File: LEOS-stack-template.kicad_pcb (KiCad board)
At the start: 2 copper layers, 100 x 100 mm, 19 parts, among them J1 MicroFit_1x4, J2 MicroFit_1x4, U1 MCP2562FD, U2 MCP2518FD, Y1 40 MHz

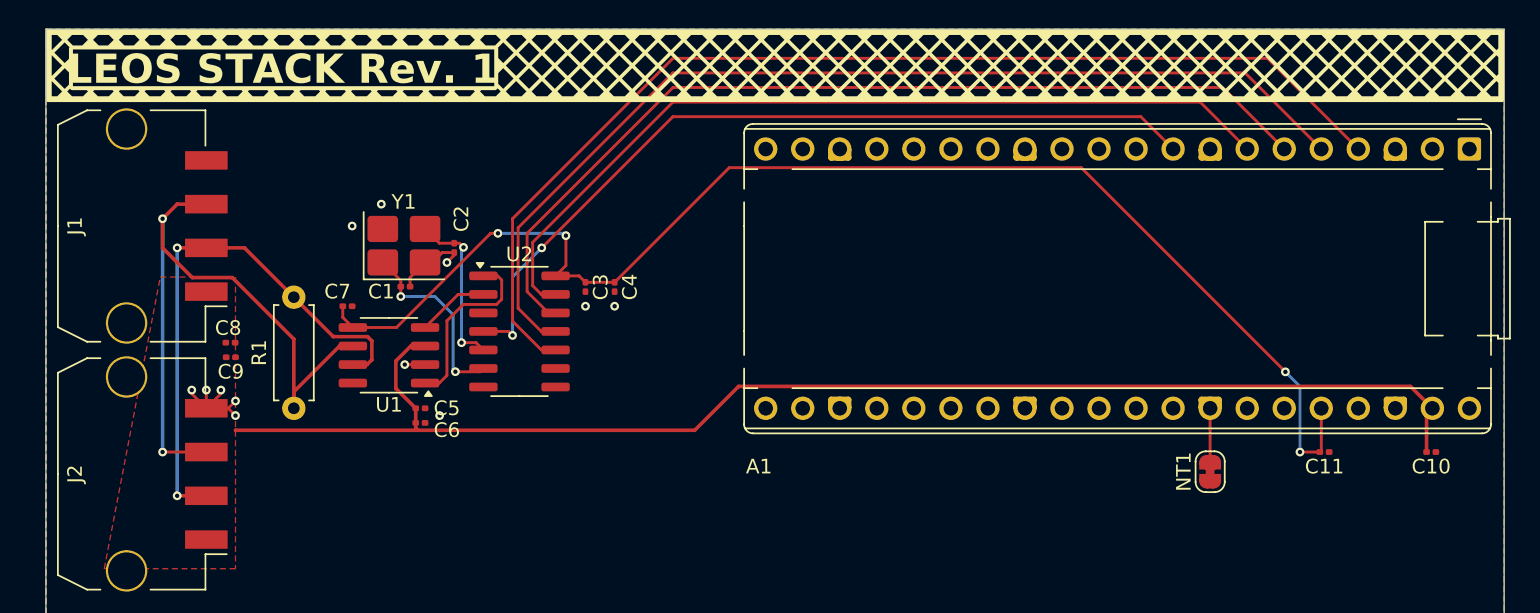
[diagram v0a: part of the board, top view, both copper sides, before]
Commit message: Redesigned Rev 2 fixing 0603 cap size and layout
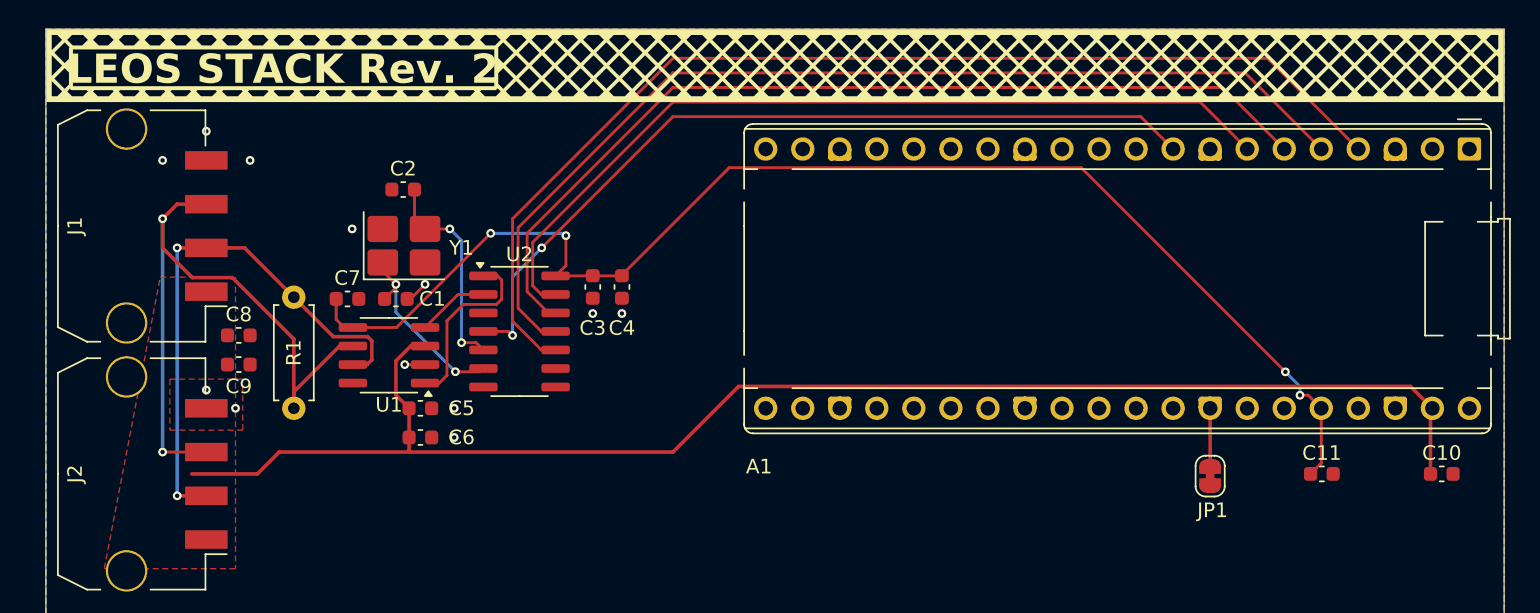
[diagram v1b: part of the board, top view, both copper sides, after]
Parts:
- removed NT1: NetTie_2, Jumper:SolderJumper-2_P1.3mm_Bridged_RoundedPad1.0x1.5mm
- added JP1: AGND Tie, Jumper:SolderJumper-2_P1.3mm_Bridged_RoundedPad1.0x1.5mm, F.Cu at (179.8, 80.7)
- C1, C10, C11, C2, C3, C4, C5, C6, C7, C8, C9: footprint Capacitor_SMD:C_0201_0603Metric -> Capacitor_SMD:C_0603_1608Metric
- moved C2 5.32 mm to (124.5, 61.0), turned to 0 degrees
- moved C10 1.67 mm to (195.7, 80.5)
- moved C11 1.51 mm to (187.5, 80.5)
- moved C1 1.07 mm to (124.0, 68.5)
- moved C6 1.00 mm to (125.7, 78.0)
- moved C8 0.76 mm to (113.2, 71.0)
- moved C9 0.74 mm to (113.2, 73.0)
- moved C3 0.50 mm to (137.5, 67.7)
- moved C4 0.50 mm to (139.5, 67.7)
- moved C7 0.50 mm to (120.7, 68.5)
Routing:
- net GND: track 14.1 -> 4.24 mm
- net +5V: track 94.9 -> 102.2 mm
- net /OSC2: track 11.5 -> 15.3 mm
- net VDD: track 91.8 -> 90.8 mm
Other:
- board text added: "LEOS STACK Rev. 2"
- board text removed: "LEOS STACK Rev. 1"

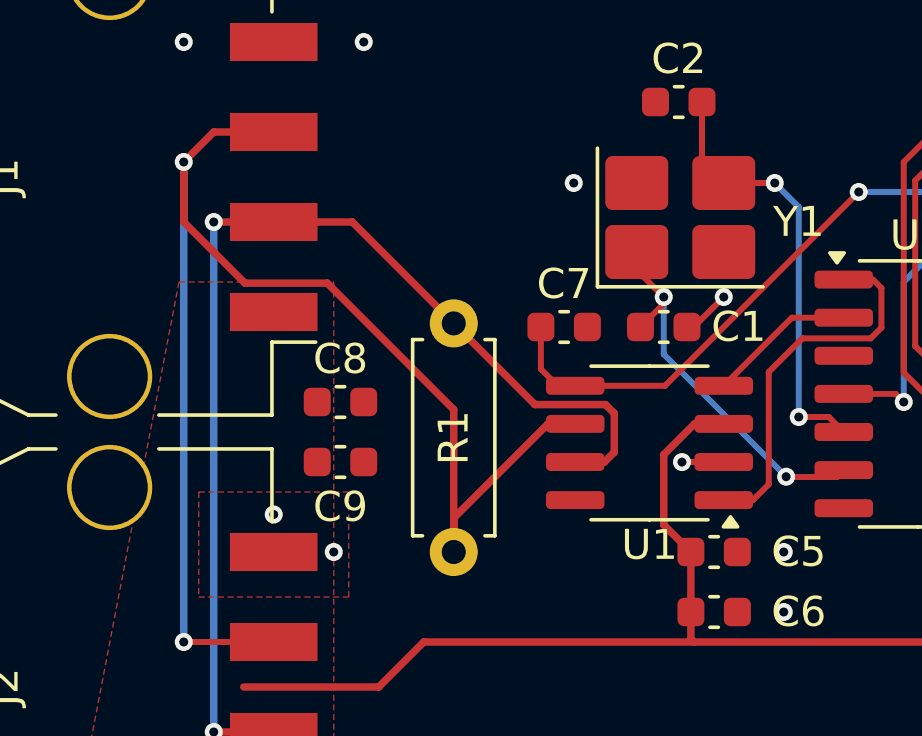
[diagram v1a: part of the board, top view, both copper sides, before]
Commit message: Clean up tracks to remove warnings
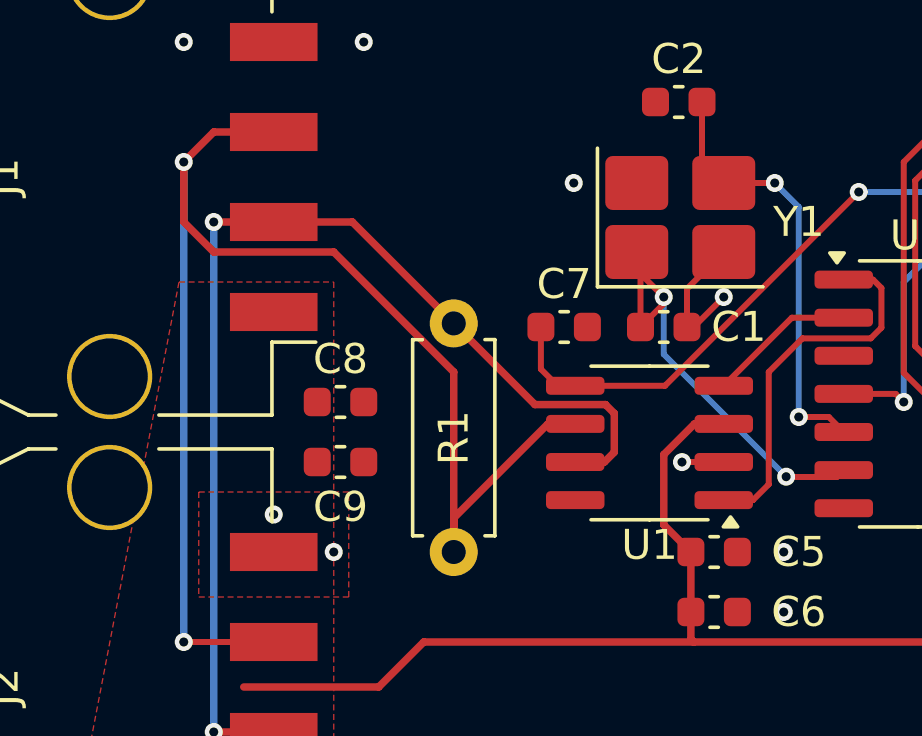
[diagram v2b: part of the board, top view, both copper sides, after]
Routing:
- net /OSC1: track 12.9 -> 15.4 mm
- net GND: track 4.24 -> 6.54 mm
- net /OSC2: track 15.3 -> 14.5 mm
- net /CAN-: track 47.2 -> 48.0 mm
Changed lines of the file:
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@@
+	)
+	(segment
+		(start 124.775 68.5)
+		(end 124.775 67.225)
+		(width 0.2)
+		(layer "F.Cu")
+		(net 13)
 	)
 	(segment
@@
 	)
 	(segment
-		(start 126.5 66.5)
-		(end 126 66)
-		(width 0.2)
-		(layer "F.Cu")
-		(net 13)
-	)
-	(segment
 		(start 124.775 68.5)
 		(end 125 68.5)
@@
 		(net 13)
 	)
+	(segment
+		(start 124.775 67.225)
+		(end 126 66)
+		(width 0.2)
+		(layer "F.Cu")
+		(net 13)
+	)
 	(via
 		(at 128 76)
@@
 	)
 	(segment
-		(start 125 76)
-		(end 125.18 75.82)
-		(width 0.25)
-		(layer "F.Cu")
-		(net 34)
-	)
-	(segment
 		(start 125 79)
 		(end 143 79)
@@
 	)
 	(segment
-		(start 124.905 76)
-		(end 125 76)
-		(width 0.25)
-		(layer "F.Cu")
-		(net 34)
-	)
-	(segment
 		(start 116 79)
 		(end 114.5 80.5)
@@
 	)
 	(segment
+		(start 123.225 66.125)
+		(end 123.1 66)
+		(width 0.2)
+		(layer "F.Cu")
+		(net 35)
+	)
+	(segment
 		(start 123.1 66)
 		(end 123.1 66.6)
@@
 	)
 	(segment
+		(start 123.225 68.5)
+		(end 123.225 66.125)
+		(width 0.2)
+		(layer "F.Cu")
+		(net 35)
+	)
+	(segment
 		(start 128.090209 73.5)
 		(end 129.77 73.5)
@@
 	)
 	(segment
-		(start 126.525 64.225)
-		(end 126 63.7)
-		(width 0.2)
-		(layer "F.Cu")
-		(net 36)
-	)
-	(segment
 		(start 125.275 61)
 		(end 125.275 62.975)
@@
 	)
 	(segment
+		(start 113 66)
+		(end 117 70)
+		(width 0.25)
+		(layer "F.Cu")
+		(net 38)
+	)
+	(segment
 		(start 111 62)
 		(end 109 62)
@@
 	)
 	(segment
-		(start 117 71.253)
-		(end 117 76)
-		(width 0.25)
-		(layer "F.Cu")
-		(net 38)
-	)
-	(segment
 		(start 117 74.86863)
 		(end 120.13863 71.73)
@@
 	)
 	(segment
-		(start 110.039 67.039)
-		(end 112.786 67.039)
-		(width 0.25)
-		(layer "F.Cu")
-		(net 38)
-	)
-	(segment
-		(start 108 65)
-		(end 110.039 67.039)
+		(start 117 70)
+		(end 117 76)
+		(width 0.25)
+		(layer "F.Cu")
+		(net 38)
+	)
+	(segment
+		(start 108 63)
+		(end 108 65)
 		(width 0.25)
 		(layer "F.Cu")
@@
 	)
 	(segment
-		(start 112.786 67.039)
-		(end 117 71.253)
-		(width 0.25)
-		(layer "F.Cu")
-		(net 38)
-	)
-	(segment
 		(start 120.13863 71.73)
 		(end 121.05 71.73)
@@
 	)
 	(segment
-		(start 108 63)
-		(end 108 65)
+		(start 109 66)
+		(end 113 66)
+		(width 0.25)
+		(layer "F.Cu")
+		(net 38)
+	)
+	(segment
+		(start 108 65)
+		(end 109 66)
 		(width 0.25)
 		(layer "F.Cu")
@@
 		(net_name "")
 		(layers "*.SilkS")
-		(hatch full 0.5)
+		(hatch edge 0.5)
 		(connect_pads
 			(clearance 0)

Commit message: New redesign featuring updated components, new sheets, better routing, and 100% 3D View
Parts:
- removed JP1: AGND Tie, Jumper:SolderJumper-2_P1.3mm_Bridged_RoundedPad1.0x1.5mm
- added TP1: CAN-H Test Point, TestPoint:TestPoint_Loop_D2.60mm_Drill0.9mm_Beaded, F.Cu at (117.0, 79.0)
- added TP2: CAN-L Test Point, TestPoint:TestPoint_Loop_D2.60mm_Drill0.9mm_Beaded, F.Cu at (117.0, 65.0)
- added TP3: 5V Test Point, TestPoint:TestPoint_Loop_D2.60mm_Drill0.9mm_Beaded, F.Cu at (117.0, 85.0)
- added TP4: GND Test Point, TestPoint:TestPoint_Loop_D2.60mm_Drill0.9mm_Beaded, F.Cu at (117.0, 59.0)
- A1: value RaspberryPi_Pico -> RaspberryPi Pico
- C1, C2: value 12pF -> 15p
- C10, C3, C5, C7: value 0.1uF -> 0.1u
- C11: value 10uF -> 10u; footprint Capacitor_SMD:C_0603_1608Metric -> Capacitor_SMD:C_0805_2012Metric
- C4, C6: value 1uF -> 1u
- C8: value 47uF -> 22u; footprint Capacitor_SMD:C_0603_1608Metric -> Capacitor_SMD:C_0805_2012Metric
- C9: value 0.1uF -> 22u; footprint Capacitor_SMD:C_0603_1608Metric -> Capacitor_SMD:C_0805_2012Metric
- J1, J2: footprint Connector_Molex:Molex_Micro-Fit_3.0_43650-0410_1x04-1MP_P3.00mm_Horizontal_PnP -> LEOS:Molex_MicroFit3.0_43650-0410_1x04_Horizontal
- R1: value 120R -> 120
- Y1: footprint Crystal:Crystal_SMD_3225-4Pin_3.2x2.5mm_HandSoldering -> Crystal:Crystal_SMD_2016-4Pin_2.0x1.6mm
- moved R1 7.81 mm to (117.0, 68.2), turned to -90 degrees
- moved C2 2.51 mm to (124.7, 63.5)
- moved C11 1.12 mm to (188.5, 80.0)
- moved Y1 1.11 mm to (124.7, 66.0)
- moved C10 0.50 mm to (195.8, 80.0)
- moved C8 0.50 mm to (113.2, 70.5)
- moved C9 0.50 mm to (113.2, 73.5)
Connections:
- net /CAN+ renamed /CANbus/CAN+
- net /CAN- renamed /CANbus/CAN-
- net /CAN_CS renamed /CANbus/CS
- net /CAN_INT renamed /CANbus/INT
- net /CAN_MISO renamed /CANbus/MISO
- net /CAN_MOSI renamed /CANbus/MOSI
- net /CAN_SCK renamed /CANbus/SCK
- net /OSC2 renamed /CANbus/OSC2
- net /RXCAN renamed Net-(U1-RXD)
- net /TXCAN renamed Net-(U1-TXD)
- A1 pad 1: UART0_TX -> unconnected-(A1-GPIO0-Pad1)
- A1 pad 10: GP7 -> unconnected-(A1-GPIO7-Pad10)
- A1 pad 11: I2C0_SDA -> unconnected-(A1-GPIO8-Pad11)
- A1 pad 12: I2C0_SCL -> unconnected-(A1-GPIO9-Pad12)
- A1 pad 14: GP10 -> unconnected-(A1-GPIO10-Pad14)
- A1 pad 15: GP11 -> unconnected-(A1-GPIO11-Pad15)
- A1 pad 16: GP12 -> unconnected-(A1-GPIO12-Pad16)
- A1 pad 17: GP13 -> unconnected-(A1-GPIO13-Pad17)
- A1 pad 19: GP14 -> unconnected-(A1-GPIO14-Pad19)
- A1 pad 2: UART0_RX -> unconnected-(A1-GPIO1-Pad2)
- A1 pad 20: GP15 -> unconnected-(A1-GPIO15-Pad20)
- A1 pad 21: GP16 -> unconnected-(A1-GPIO16-Pad21)
- A1 pad 22: GP17 -> unconnected-(A1-GPIO17-Pad22)
- A1 pad 24: GP18 -> unconnected-(A1-GPIO18-Pad24)
- A1 pad 25: GP19 -> unconnected-(A1-GPIO19-Pad25)
- A1 pad 26: GP20 -> unconnected-(A1-GPIO20-Pad26)
- A1 pad 27: GP21 -> unconnected-(A1-GPIO21-Pad27)
- A1 pad 29: GP22 -> unconnected-(A1-GPIO22-Pad29)
- A1 pad 30: RUN -> unconnected-(A1-RUN-Pad30)
- A1 pad 31: ADC0 -> unconnected-(A1-GPIO26_ADC0-Pad31)
- A1 pad 32: ADC1 -> unconnected-(A1-GPIO27_ADC1-Pad32)
- A1 pad 33: Net-(A1-AGND) -> unconnected-(A1-AGND-Pad33)
- A1 pad 34: ADC2 -> unconnected-(A1-GPIO28_ADC2-Pad34)
- C1 pad 1: /OSC1 -> GND
- C1 pad 2: GND -> /CANbus/OSC1
- U2 pad 6: /OSC1 -> /CANbus/OSC1
- Y1 pad 1: /OSC1 -> /CANbus/OSC1
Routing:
- net /OSC1: track 15.4 -> 0.00 mm, vias 2 -> 0
- net /CANbus/OSC1: track 0.00 -> 11.1 mm, vias 0 -> 2
- net /CANbus/CAN-: track 48.0 -> 39.1 mm
- net VDD: track 90.8 -> 98.4 mm, vias 4 -> 3
- net +5V: track 101.8 -> 107.8 mm
- net GND: track 6.54 -> 1.39 mm, vias 12 -> 21
- net /CANbus/CAN+: track 37.7 -> 42.3 mm
- net Net-(A1-AGND): track 4.00 -> 0.00 mm
- net /CANbus/INT: track 56.9 -> 59.1 mm
- net /CANbus/CS: track 59.1 -> 61.2 mm
- net /CANbus/OSC2: track 14.5 -> 12.5 mm
- net /CANbus/MISO: track 64.4 -> 65.3 mm
- net /CANbus/MOSI: track 70.4 -> 71.1 mm
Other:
- board text added: "5V"
- board text added: "CAN-H"
- board text added: "CAN-L"
- board text added: "GND"
- board text added: "LEOS CHANGE THIS NAME Rev. 3"
- board text removed: "LEOS STACK Rev. 2"

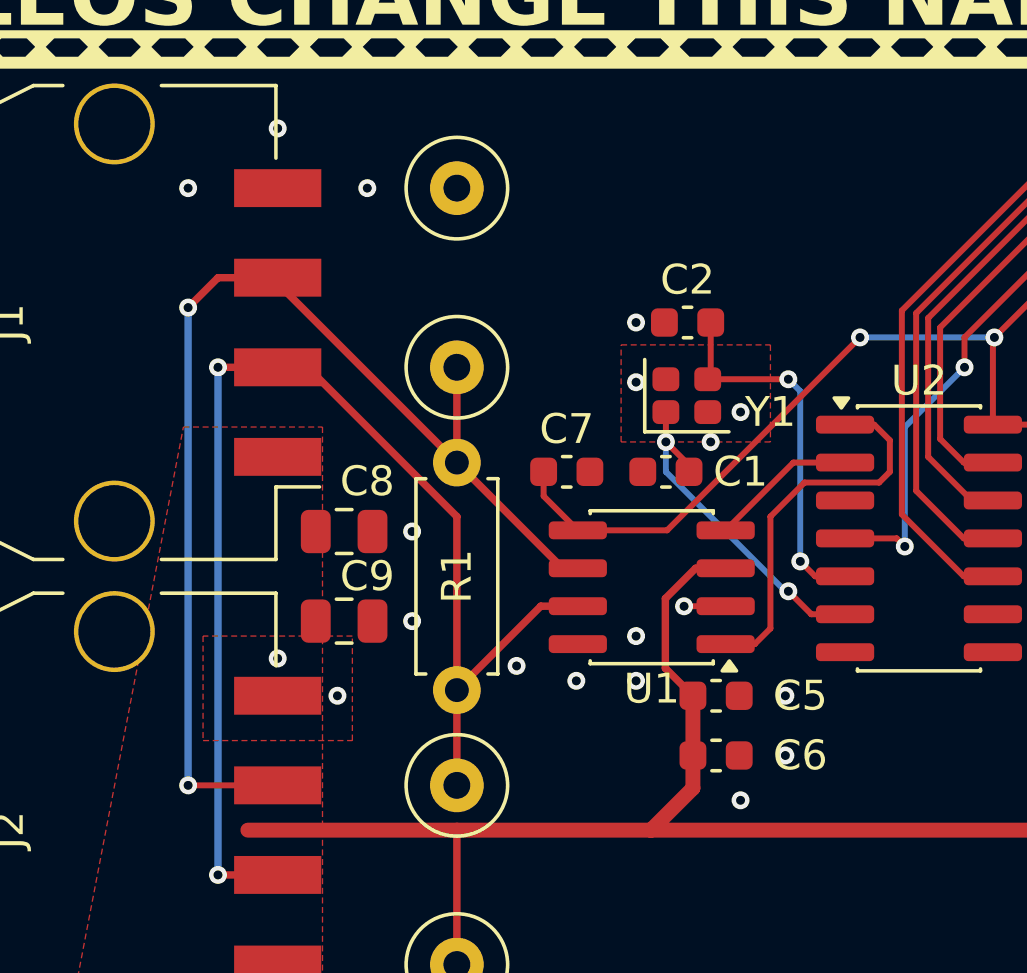
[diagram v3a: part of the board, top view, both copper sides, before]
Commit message: Improved via placement, added LCSC part numbers.
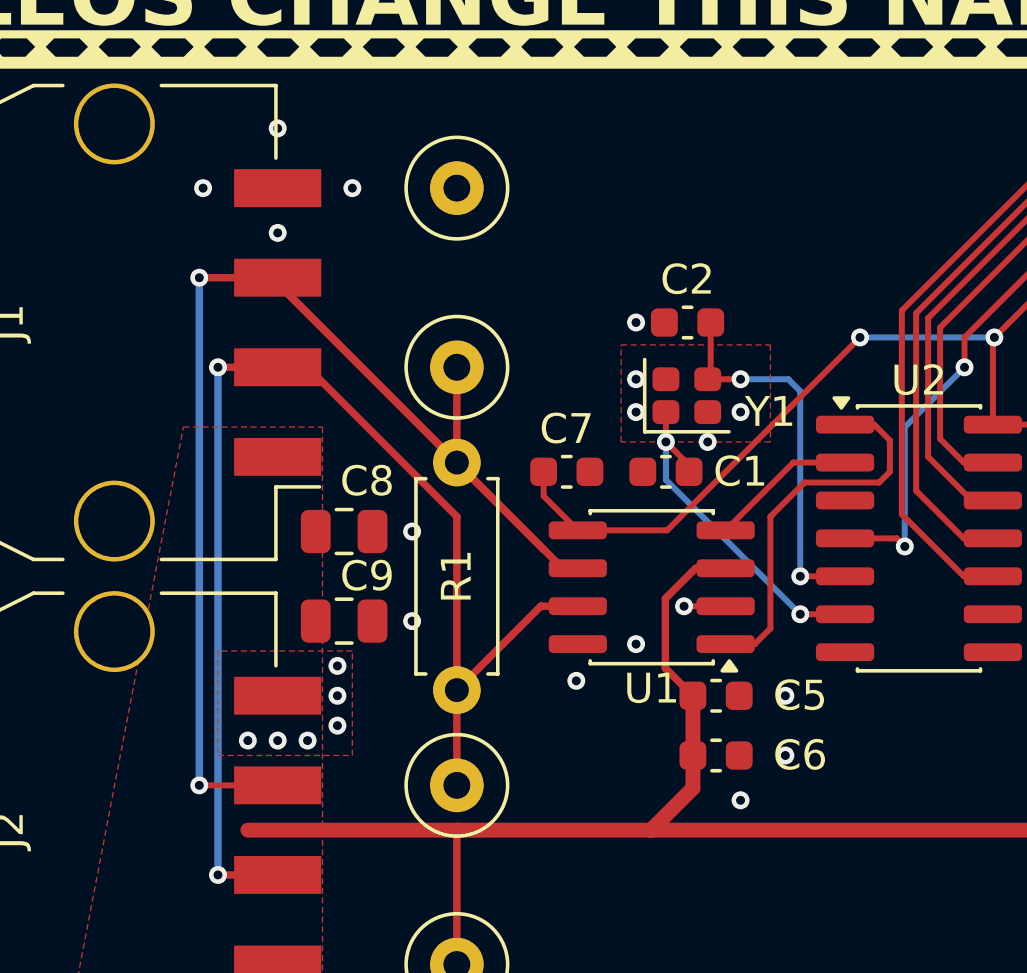
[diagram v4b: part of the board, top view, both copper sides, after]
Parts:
- C1, C2: value 15p -> 10p
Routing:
- net /CANbus/CAN-: track 39.1 -> 51.3 mm
- net GND: vias 21 -> 25

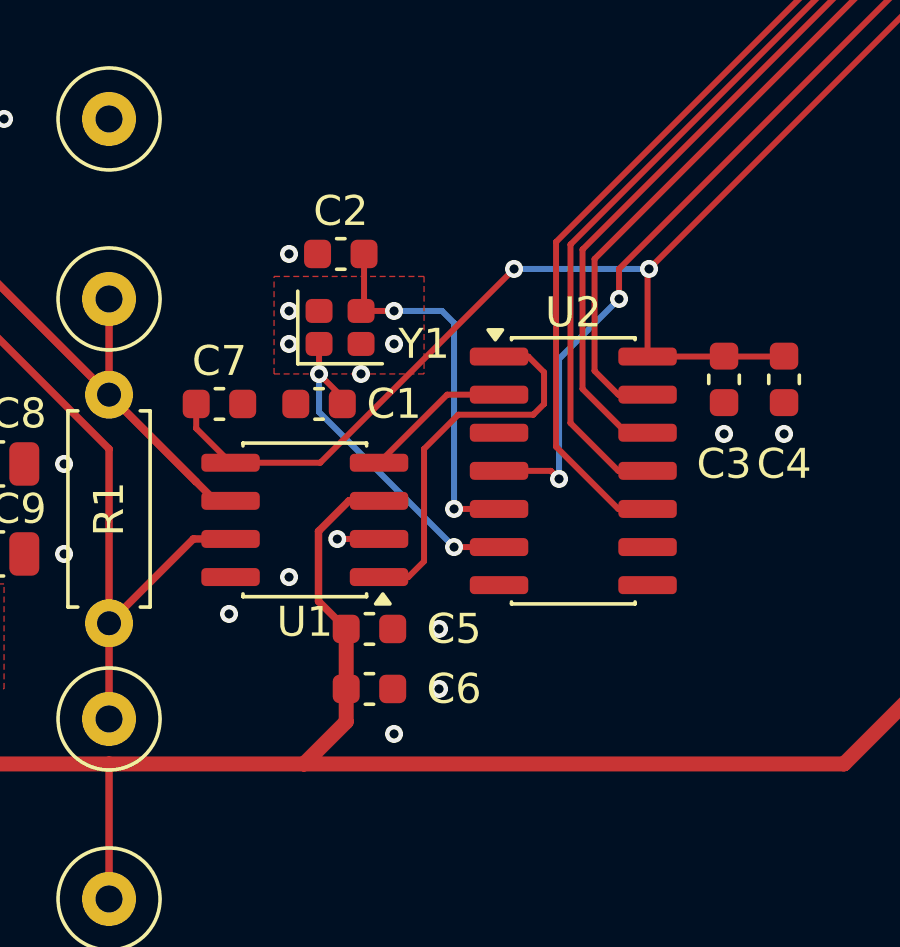
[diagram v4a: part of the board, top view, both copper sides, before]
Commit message: Updated routing for CANbus crystal. Should improve stencil process.
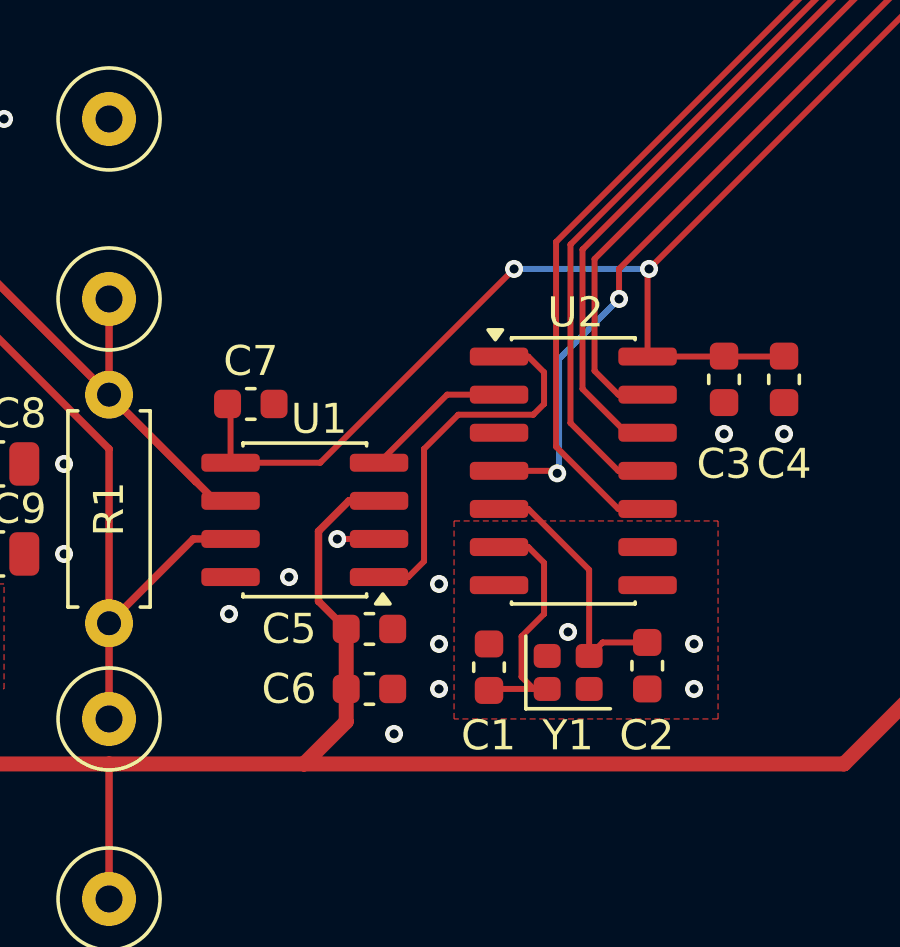
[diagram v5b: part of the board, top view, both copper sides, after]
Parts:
- moved C2 17.1 mm to (134.9, 77.2), turned to 90 degrees
- moved Y1 13.8 mm to (132.3, 77.5)
- moved C1 10.4 mm to (129.7, 77.3), turned to -90 degrees
- moved C7 1.04 mm to (121.7, 68.5)
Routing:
- net /CANbus/OSC2: track 12.8 -> 8.84 mm, vias 2 -> 0
- net /CANbus/OSC1: track 11.2 -> 8.74 mm, vias 2 -> 0
- net VDD: track 98.4 -> 97.8 mm
- net GND: vias 25 -> 24
